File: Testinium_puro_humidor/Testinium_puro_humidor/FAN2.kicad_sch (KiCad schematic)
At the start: 0 parts

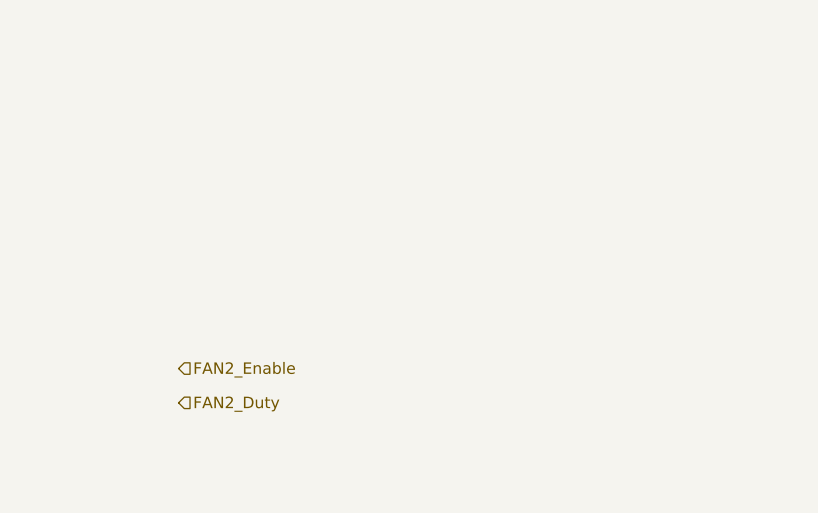
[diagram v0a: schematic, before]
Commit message: fan , uv led ,regülator devresi eklendi. piezo ve sarj devresi kaldi
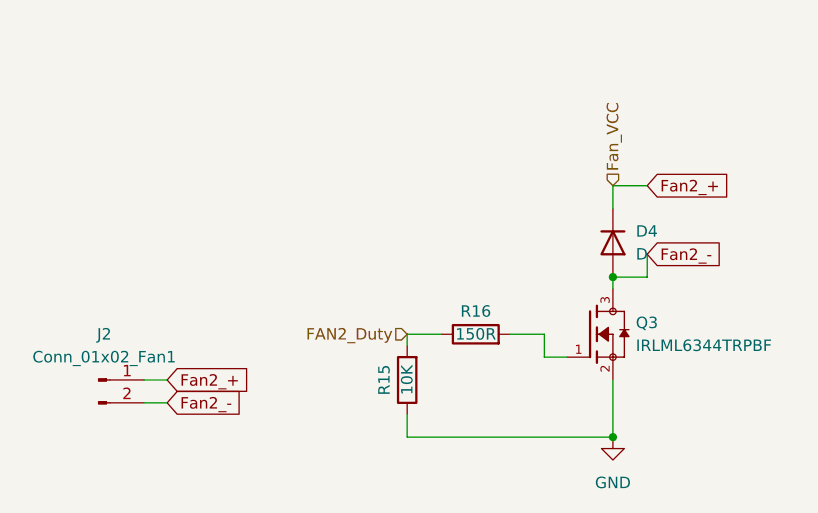
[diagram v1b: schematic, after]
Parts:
- added D4: D, symbol Device:D
- added J2: Conn_01x02_Fan1, Connector_JST:JST_EH_B2B-EH-A_1x02_P2.50mm_Vertical, symbol Connector:Conn_01x02_Pin
- added Q3: IRLML6344TRPBF, baraysan:TRANS_IRLML6344TRPBF, symbol BARAYSAN:IRLML6344TRPBF
- added R15: 10K, symbol Device:R
- added R16: 150R, symbol Device:R
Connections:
- net FAN2_Duty: now also R15.2, R16.1
- new net: Q3.1, R16.2
- new net Fan2_+: D4.1 (K), J2.1 (Pin_1)
- new net Fan2_-: D4.2 (A), J2.2 (Pin_2), Q3.3
- new net GND: Q3.2, R15.1

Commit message: sematik tamamlandi
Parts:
- added R26: 0R, Resistor_SMD:R_0603_1608Metric, symbol Device:R
- D4: footprint (none) -> Diode_SMD:D_SMA
- R15, R16: footprint (none) -> Resistor_SMD:R_0805_2012Metric
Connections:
- net Fan2_+: now also R26.1
- new net Fan_VCC: R26.2
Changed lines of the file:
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@@
+	)
+	(junction
+		(at 87.63 31.75)
+		(diameter 0)
+		(color 0 0 0 0)
 	)
 	(junction
@@
 	(wire
 		(pts
-			(xy 87.63 31.75) (xy 87.63 29.21)
-		)
-		(stroke
-			(width 0)
-			(type default)
-		)
-	)
-	(wire
-		(pts
-			(xy 87.63 29.21) (xy 91.44 29.21)
+			(xy 87.63 31.75) (xy 91.44 31.75)
+		)
+		(stroke
+			(width 0)
+			(type default)
+		)
+	)
+	(wire
+		(pts
+			(xy 87.63 21.59) (xy 87.63 24.13)
 		)
 		(stroke
@@
 	(global_label "Fan2_+"
 		(shape input)
-		(at 91.44 29.21 0)
+		(at 91.44 31.75 0)
 		(fields_autoplaced yes)
 		(effects
@@
 		)
 		(property "Intersheetrefs" "${INTERSHEET_REFS}"
-			(at 101.5613 29.21 0)
+			(at 101.5613 31.75 0)
 			(effects
 				(font
@@
 	(hierarchical_label "Fan_VCC"
 		(shape input)
-		(at 87.63 29.21 90)
+		(at 87.63 21.59 90)
 		(effects
 			(font
@@
 			)
 			(justify right)
+		)
+	)
+	(symbol
+		(lib_id "Device:R")
+		(at 87.63 27.94 180)
+		(unit 1)
+		(exclude_from_sim no)
+		(in_bom yes)
+		(on_board yes)
+		(dnp no)
+		(property "Reference" "R26"
+			(at 85.09 27.94 90)
+			(effects
+				(font
+					(size 1.27 1.27)
+				)
+			)
+		)
+		(property "Value" "0R"
+			(at 87.63 27.94 90)
+			(effects
+				(font
+					(size 1.27 1.27)
+				)
+			)
+		)
+		(property "Footprint" "Resistor_SMD:R_0603_1608Metric"
+			(at 89.408 27.94 90)
+			(effects
+				(font
+					(size 1.27 1.27)
+				)
+				(hide yes)
+			)
+		)
+		(property "Datasheet" "~"
+			(at 87.63 27.94 0)
+			(effects
+				(font
+					(size 1.27 1.27)
+				)
+				(hide yes)
+			)
+		)
+		(property "Description" "Resistor"
+			(at 87.63 27.94 0)
+			(effects
+				(font
+					(size 1.27 1.27)
+				)
+				(hide yes)
+			)
+		)
+		(property "HHH" ""
+			(at 87.63 27.94 0)
+			(effects
+				(font
+					(size 1.27 1.27)
+				)
+				(hide yes)
+			)
+		)
+		(pin "1"
+		)
+		(pin "2"
+		)
+		(instances
+			(project "Testinium_puro_humidor"
+				(path "/eaf24445-473d-4e1b-a90d-ef2c4a02e74f/5c9c0f3a-6ea9-4000-af5c-25fa8998a29b"
+					(reference "R26")
+					(unit 1)
+				)
+			)
 		)
 	)
@@
 			)
 		)
-		(property "Footprint" ""
+		(property "Footprint" "Diode_SMD:D_SMA"
 			(at 87.63 35.56 0)
 			(effects
@@
 			)
 		)
-		(property "Footprint" ""
+		(property "Footprint" "Resistor_SMD:R_0805_2012Metric"
 			(at 72.39 47.498 90)
 			(effects
@@
 			)
 		)
-		(property "Footprint" ""
+		(property "Footprint" "Resistor_SMD:R_0805_2012Metric"
 			(at 66.548 50.8 90)
 			(effects
